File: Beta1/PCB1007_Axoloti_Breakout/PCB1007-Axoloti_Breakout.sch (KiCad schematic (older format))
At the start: 35 parts, among them J1 Axoloti_40Pin, U10 OLED_128x32_I2C, U1000 MCP3008T-I/SL, U2 MCP3008T-I/SL, U20 OLED_128x32_I2C, U30 OLED_128x32_I2C, U40 OLED_128x32_I2C, U5 I2C_1x4MUX_TCA9546A

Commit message: SCH+Route complete
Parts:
- removed C1, C1000, C2: 0.1u, Capacitors_SMD:C_0603, symbol C
- removed JOY0, JOY1, JOY2, JOY3: XYJOY, Liberry:XY_JOY_254TA103B50B, symbol XYJOY
- removed RC0, RC10, RC20, RC30, RC40, RD0, RD10, RD20, RD30, RD40, RR0: 10K, Resistors_SMD:R_0603, symbol R
- removed RV0, RV1, RV2, RV3, RV4, RV5, RV6, RV7, RV_VOL1: POT, Liberry:RV09AF-40-20K-B10K, symbol POT
- removed U10, U20, U30, U40: OLED_128x32_I2C, Liberry:OLED_128x32, symbol OLED_128x32_I2C
- removed U1000, U2: MCP3008T-I/SL, Liberry:SOIC-16, symbol MCP3008T-I/SL
- removed U5: I2C_1x4MUX_TCA9546A, Liberry:SOIC-16_1.27x5.4, symbol I2C_1x4MUX_TCA9546A
- added JK0: USB-K, Liberry:USB-K_12401610E4_2A, symbol USB-K
- added TEST0, TEST1, TEST2: CONN_01X01, Liberry:TH_0.1_1x2_Jumper, symbol CONN_01X01
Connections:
- net labels added: JOY0, JOY1, JOY_SW, RX, TEST0, TEST1, TEST2, TX
- net labels removed: I2C_SCL0, I2C_SCL1, I2C_SCL2, I2C_SCL3, I2C_SDA0, I2C_SDA1, I2C_SDA2, I2C_SDA3, JOY_0_0, JOY_0_1, JOY_0_SW, JOY_1_0, JOY_1_1, JOY_2_0, JOY_2_1, JOY_3_0, JOY_3_1, JOY_K0, JOY_K1, P0, P1, P2, P3, P4, P5, P6, P7
- wire segments 204 -> 60

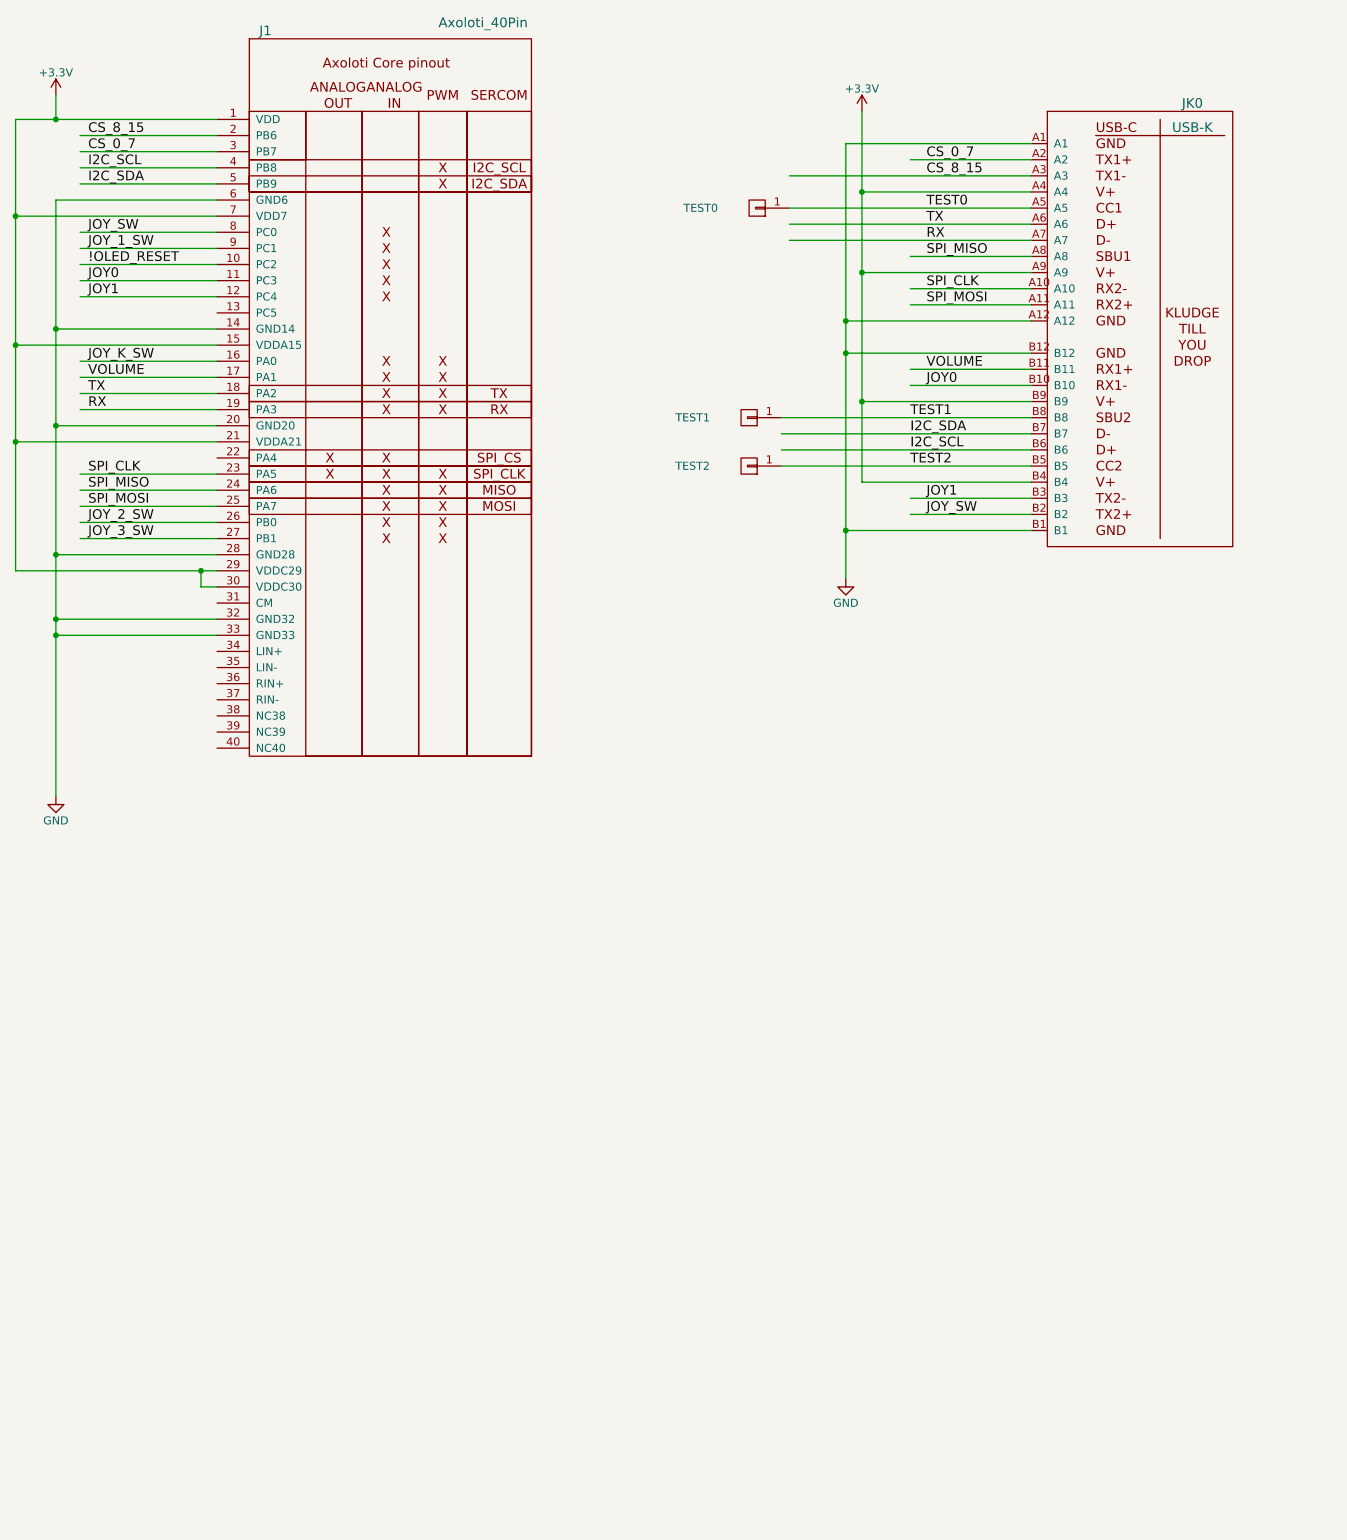
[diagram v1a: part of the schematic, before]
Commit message: Conversion to FFC WIP
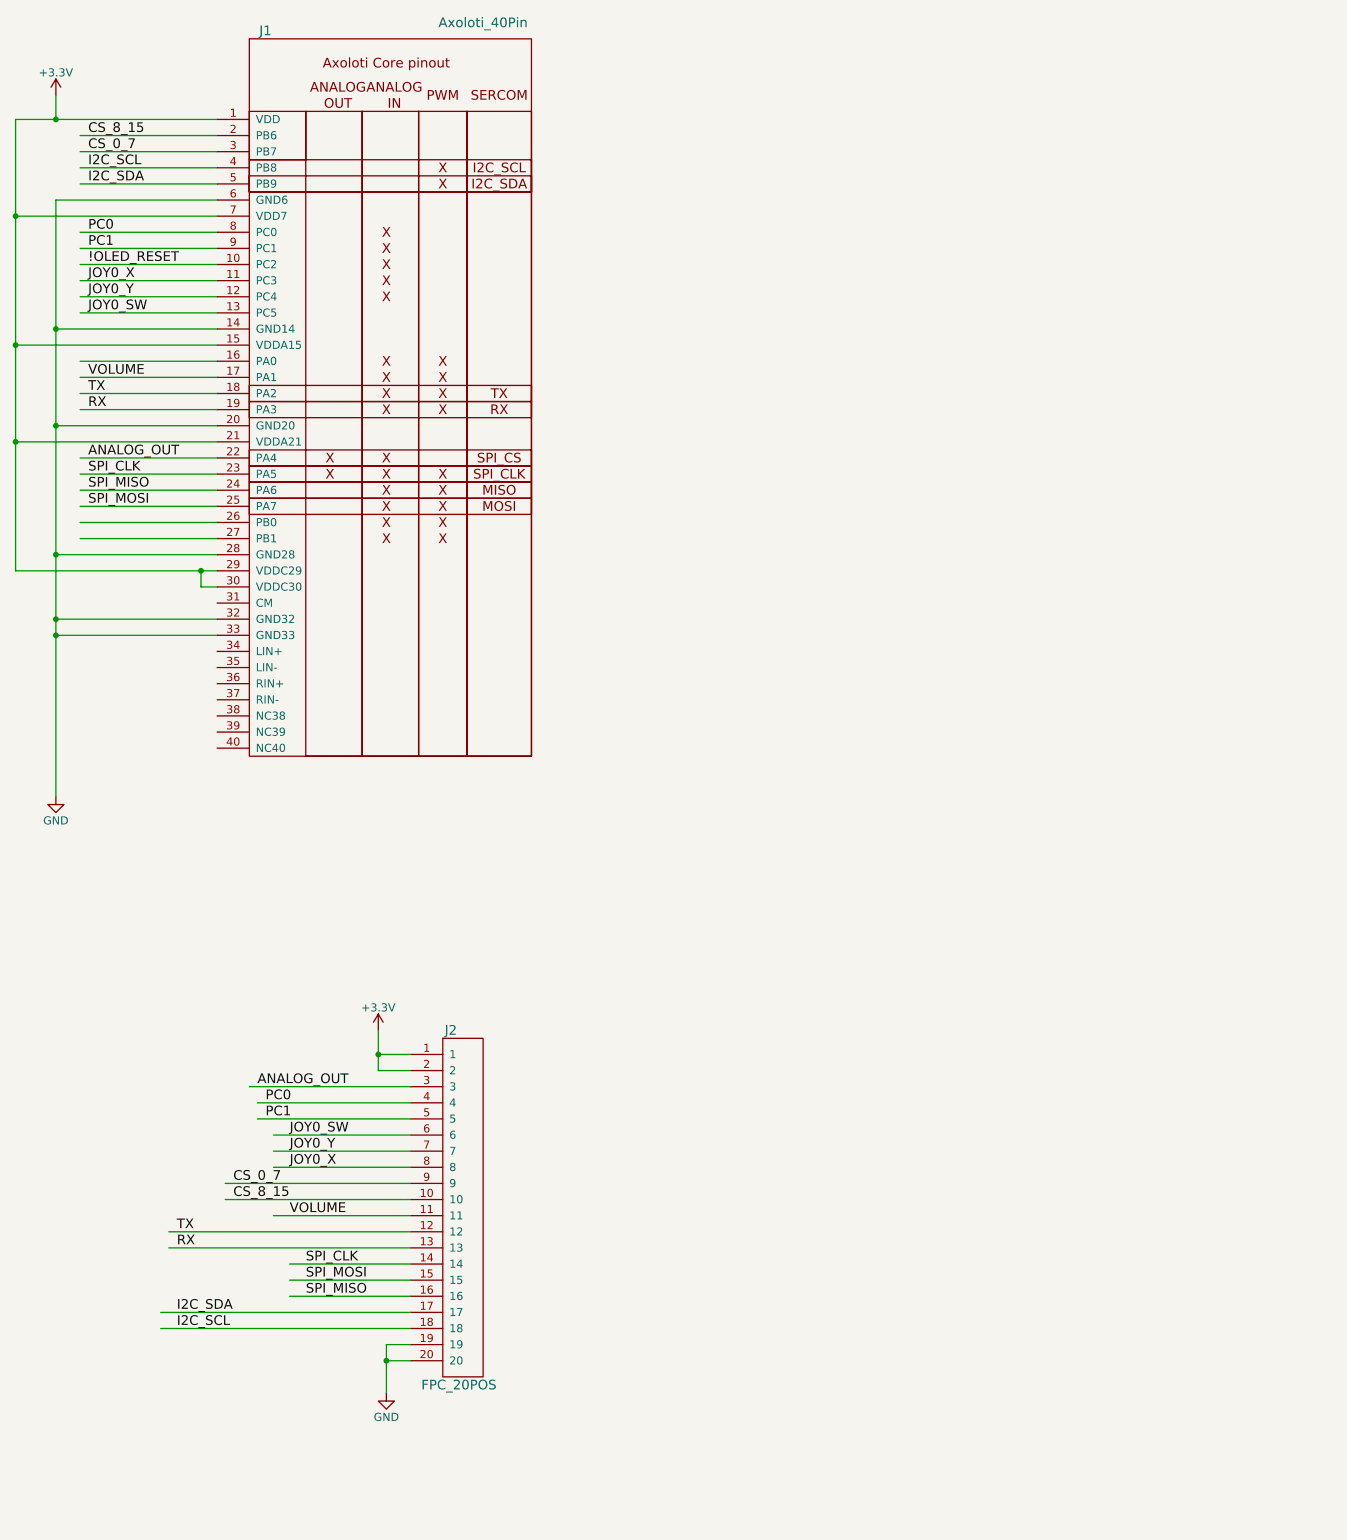
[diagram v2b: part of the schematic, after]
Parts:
- removed JK0: USB-K, Liberry:USB-K_12401610E4_2A, symbol USB-K
- removed TEST0, TEST1, TEST2: CONN_01X01, Liberry:TH_0.1_1x2_Jumper, symbol CONN_01X01
- added J2: FPC_20POS, Liberry:FFC_1MM_20POS_MOLEX_52271-2079, symbol FPC_20POS
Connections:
- net labels added: ANALOG_OUT, JOY0_SW, JOY0_X, JOY0_Y, PC0, PC1
- net labels removed: JOY0, JOY1, JOY_1_SW, JOY_2_SW, JOY_3_SW, JOY_K_SW, JOY_SW, TEST0, TEST1, TEST2
- wire segments 60 -> 58
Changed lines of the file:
@@
 Text Label 15100 4300 0    60   ~ 0
 SPI_CLK
-Text Label 15100 2800 0    60   ~ 0
-JOY_SW
-Text Label 15100 2900 0    60   ~ 0
-JOY_1_SW
-Text Label 15100 4600 0    60   ~ 0
-JOY_2_SW
 Text Label 15100 2300 0    60   ~ 0
 CS_0_7
@@
 Text Label 15100 3000 0    60   ~ 0
 !OLED_RESET
+Text Label 15100 3700 0    60   ~ 0
+VOLUME
+Text Label 15100 3100 0    60   ~ 0
+JOY0_X
+Text Label 15100 3200 0    60   ~ 0
+JOY0_Y
+Text Label 16450 9300 0    60   ~ 0
+SPI_MOSI
+Text Label 16450 9200 0    60   ~ 0
+SPI_CLK
+Text Label 16000 8700 0    60   ~ 0
+CS_0_7
+Text Label 16350 8900 0    60   ~ 0
+VOLUME
+Text Label 16350 8600 0    60   ~ 0
+JOY0_X
+Text Label 15650 9600 0    60   ~ 0
+I2C_SCL
+Text Label 15650 9500 0    60   ~ 0
+I2C_SDA
+Text Label 15650 9100 0    60   ~ 0
+RX
+Text Label 15650 9000 0    60   ~ 0
+TX
+Text Label 16000 8800 0    60   ~ 0
+CS_8_15
+Text Label 16450 9400 0    60   ~ 0
+SPI_MISO
+Text Label 15100 3800 0    60   ~ 0
+TX
+Text Label 15100 3900 0    60   ~ 0
+RX
+$Comp
+L +3.3V #PWR?
+U 1 1 596EA01A
+P 16900 7750
+F 0 "#PWR?" H 16900 7600 50  0001 C CNN
+F 1 "+3.3V" H 16900 7890 50  0000 C CNN
+F 2 "" H 16900 7750 50  0000 C CNN
+F 3 "" H 16900 7750 50  0000 C CNN
+	1    16900 7750
+	1    0    0    -1
+$EndComp
+$Comp
+L GND #PWR?
+U 1 1 596EA0DD
+P 16950 10000
+F 0 "#PWR?" H 16950 9750 50  0001 C CNN
+F 1 "GND" H 16950 9850 50  0000 C CNN
+F 2 "" H 16950 10000 50  0000 C CNN
+F 3 "" H 16950 10000 50  0000 C CNN
+	1    16950 10000
+	1    0    0    -1
+$EndComp
+$Comp
+L FPC_20POS J2
+U 1 1 596EA301
+P 17300 7900
+F 0 "J2" H 17350 8050 60  0000 C CNN
+F 1 "FPC_20POS" H 17400 5850 60  0000 C CNN
+F 2 "Liberry:FFC_1MM_20POS_MOLEX_52271-2079" H 17100 7450 60  0001 C CNN
+F 3 "" H 17100 7450 60  0001 C CNN
+	1    17300 7900
+	1    0    0    -1
+$EndComp
+Text Label 16350 8500 0    60   ~ 0
+JOY0_Y
+Text Label 15100 3300 0    60   ~ 0
+JOY0_SW
+Text Label 16350 8400 0    60   ~ 0
+JOY0_SW
+Text Label 15100 2800 0    60   ~ 0
+PC0
+Text Label 15100 4200 0    60   ~ 0
+ANALOG_OUT
+Text Label 16150 8100 0    60   ~ 0
+ANALOG_OUT
+Text Label 15100 2900 0    60   ~ 0
+PC1
+Text Label 16200 8200 0    60   ~ 0
+PC0
+Text Label 16200 8300 0    60   ~ 0
+PC1
 Wire Wire Line
 	15050 2500 15900 2500
@@
 Wire Wire Line
 	15050 2900 15900 2900
-Wire Wire Line
-	15050 4600 15900 4600
 Wire Wire Line
 	15050 2300 15900 2300
@@
 Wire Wire Line
 	15900 4700 15050 4700
-Text Label 15100 4700 0    60   ~ 0
-JOY_3_SW
-Text Label 15100 3700 0    60   ~ 0
-VOLUME
 Wire Wire Line
 	15050 3700 15900 3700
-Text Label 15100 3100 0    60   ~ 0
-JOY0
-Text Label 15100 3200 0    60   ~ 0
-JOY1
-Text Label 15100 3600 0    60   ~ 0
-JOY_K_SW
 Wire Wire Line
 	15900 3100 15050 3100
@@
 	15900 3200 15050 3200
 Wire Wire Line
+	17100 9300 16350 9300
+Wire Wire Line
+	17100 9200 16350 9200
+Wire Wire Line
+	16350 9400 17100 9400
+Wire Wire Line
+	15600 9100 17100 9100
+Wire Wire Line
+	15600 9000 17100 9000
+Wire Wire Line
+	15950 8700 17100 8700
+Wire Wire Line
+	16250 8900 17100 8900
+Wire Wire Line
+	16250 8600 17100 8600
+Wire Wire Line
+	15550 9500 17100 9500
+Wire Wire Line
+	15550 9600 17100 9600
+Wire Wire Line
+	15900 3800 15050 3800
+Wire Wire Line
+	15900 3900 15050 3900
+Wire Wire Line
+	17100 7900 16900 7900
+Wire Wire Line
+	16900 7750 16900 8000
+Wire Wire Line
+	16900 8000 17100 8000
+Connection ~ 16900 7900
+Wire Wire Line
+	17100 9700 16950 9700
+Wire Wire Line
+	16950 9700 16950 10000
+Wire Wire Line
+	16950 9800 17100 9800
+Connection ~ 16950 9800
+Wire Wire Line
+	15950 8800 17100 8800
+Wire Wire Line
+	16250 8500 17100 8500
+Wire Wire Line
+	15050 3300 15900 3300
+Wire Wire Line
+	16250 8400 17100 8400
+Wire Wire Line
+	15050 4600 15900 4600
+Wire Wire Line
 	15900 3600 15050 3600
-$Comp
-L USB-K JK0
-U 1 1 59612141
-P 20950 3450
-F 0 "JK0" H 21950 4900 60  0000 C CNN
-F 1 "USB-K" H 21950 4750 60  0000 C CNN
-F 2 "Liberry:USB-K_12401610E4_2A" H 21000 3350 60  0001 C CNN
-F 3 "" H 21000 3350 60  0001 C CNN
-	1    20950 3450
-	1    0    0    -1
-$EndComp
-$Comp
-L GND #PWR03
-U 1 1 59612148
-P 19800 4950
-F 0 "#PWR03" H 19800 4700 50  0001 C CNN
-F 1 "GND" H 19800 4800 50  0000 C CNN
-F 2 "" H 19800 4950 50  0000 C CNN
-F 3 "" H 19800 4950 50  0000 C CNN
-	1    19800 4950
-	1    0    0    -1
-$EndComp
-$Comp
-L +3.3V #PWR04
-U 1 1 5961214E
-P 19900 2050
-F 0 "#PWR04" H 19900 1900 50  0001 C CNN
-F 1 "+3.3V" H 19900 2190 50  0000 C CNN
-F 2 "" H 19900 2050 50  0000 C CNN
-F 3 "" H 19900 2050 50  0000 C CNN
-	1    19900 2050
-	1    0    0    -1
-$EndComp
-Wire Wire Line
-	19800 4650 20950 4650
-Wire Wire Line
-	19800 2250 19800 4950
-Wire Wire Line
-	20950 3550 19800 3550
-Connection ~ 19800 4650
-Wire Wire Line
-	20950 3350 19800 3350
-Connection ~ 19800 3550
-Wire Wire Line
-	20950 2250 19800 2250
-Connection ~ 19800 3350
-Wire Wire Line
-	20950 2550 19900 2550
-Wire Wire Line
-	19900 2050 19900 4350
-Wire Wire Line
-	19900 3050 20950 3050
-Connection ~ 19900 2550
-Wire Wire Line
-	19900 3850 20950 3850
-Connection ~ 19900 3050
-Wire Wire Line
-	19900 4350 20950 4350
-Connection ~ 19900 3850
-Wire Wire Line
-	20950 3250 20200 3250
-Wire Wire Line
-	20950 3150 20200 3150
-Wire Wire Line
-	20200 2950 20950 2950
-Wire Wire Line
-	19450 2850 20950 2850
-Wire Wire Line
-	19450 2750 20950 2750
-Wire Wire Line
-	19450 2650 20950 2650
-Wire Wire Line
-	19450 2450 20950 2450
-Wire Wire Line
-	20950 2350 20200 2350
-Wire Wire Line
-	20950 3650 20200 3650
-Wire Wire Line
-	20950 3750 20200 3750
-Wire Wire Line
-	19400 3950 20950 3950
-Wire Wire Line
-	19400 4050 20950 4050
-Wire Wire Line
-	19400 4150 20950 4150
-Wire Wire Line
-	19400 4250 20950 4250
-Wire Wire Line
-	20950 4450 20200 4450
-Wire Wire Line
-	20950 4550 20200 4550
-Text Label 20300 3250 0    60   ~ 0
-SPI_MOSI
-Text Label 20300 3150 0    60   ~ 0
-SPI_CLK
-Text Label 20300 2350 0    60   ~ 0
-CS_0_7
-$Comp
-L CONN_01X01 TEST0
-U 1 1 59612194
-P 19250 2650
-F 0 "TEST0" H 19600 2650 50  0000 C CNN
-F 1 "CONN_01X01" V 19350 2650 50  0001 C CNN
-F 2 "Liberry:TH_0.1_1x2_Jumper" H 19250 2650 50  0001 C CNN
-F 3 "" H 19250 2650 50  0000 C CNN
-F 4 "PCB" H 19250 2650 60  0001 C CNN "MFG"
-F 5 "ON_PCB" H 19250 2650 60  0001 C CNN "MPN"
-	1    19250 2650
-	-1   0    0    1
-$EndComp
-Text Label 20300 3650 0    60   ~ 0
-VOLUME
-Text Label 20300 3750 0    60   ~ 0
-JOY0
-Text Label 20300 4550 0    60   ~ 0
-JOY_SW
-Text Label 20300 4450 0    60   ~ 0
-JOY1
-$Comp
-L CONN_01X01 TEST1
-U 1 1 596121B3
-P 19200 3950
-F 0 "TEST1" H 19550 3950 50  0000 C CNN
-F 1 "CONN_01X01" V 19300 3950 50  0001 C CNN
-F 2 "Liberry:TH_0.1_1x2_Jumper" H 19200 3950 50  0001 C CNN
-F 3 "" H 19200 3950 50  0000 C CNN
-F 4 "PCB" H 19200 3950 60  0001 C CNN "MFG"
-F 5 "ON_PCB" H 19200 3950 60  0001 C CNN "MPN"
-	1    19200 3950
-	-1   0    0    1
-$EndComp
-$Comp
-L CONN_01X01 TEST2
-U 1 1 596121BC
-P 19200 4250
-F 0 "TEST2" H 19550 4250 50  0000 C CNN
-F 1 "CONN_01X01" V 19300 4250 50  0001 C CNN
-F 2 "Liberry:TH_0.1_1x2_Jumper" H 19200 4250 50  0001 C CNN
-F 3 "" H 19200 4250 50  0000 C CNN
-F 4 "PCB" H 19200 4250 60  0001 C CNN "MFG"
-F 5 "ON_PCB" H 19200 4250 60  0001 C CNN "MPN"
-	1    19200 4250
-	-1   0    0    1
-$EndComp
-Text Label 20200 4150 0    60   ~ 0
-I2C_SCL
-Text Label 20200 4250 0    60   ~ 0
-TEST2
-Text Label 20200 4050 0    60   ~ 0
-I2C_SDA
-Text Label 20200 3950 0    60   ~ 0
-TEST1
-Text Label 20300 2850 0    60   ~ 0
-RX
-Text Label 20300 2750 0    60   ~ 0
-TX
-Text Label 20300 2650 0    60   ~ 0
-TEST0
-Text Label 20300 2450 0    60   ~ 0
-CS_8_15
-Text Label 20300 2950 0    60   ~ 0
-SPI_MISO
-Wire Wire Line
-	15900 3800 15050 3800
-Wire Wire Line
-	15900 3900 15050 3900
-Text Label 15100 3800 0    60   ~ 0
-TX
-Text Label 15100 3900 0    60   ~ 0
-RX
+Wire Wire Line
+	15900 4200 15050 4200
+Wire Wire Line
+	16100 8100 17100 8100
+Wire Wire Line
+	16150 8200 17100 8200
+Wire Wire Line
+	16150 8300 17100 8300
 $EndSCHEMATC

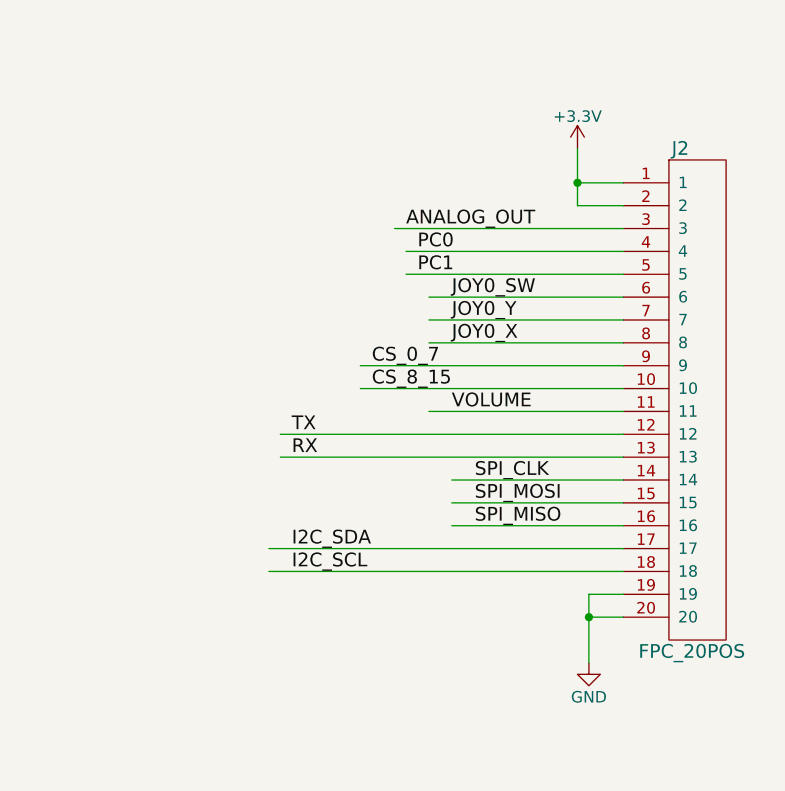
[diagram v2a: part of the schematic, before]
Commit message: Added 20 pos FFC
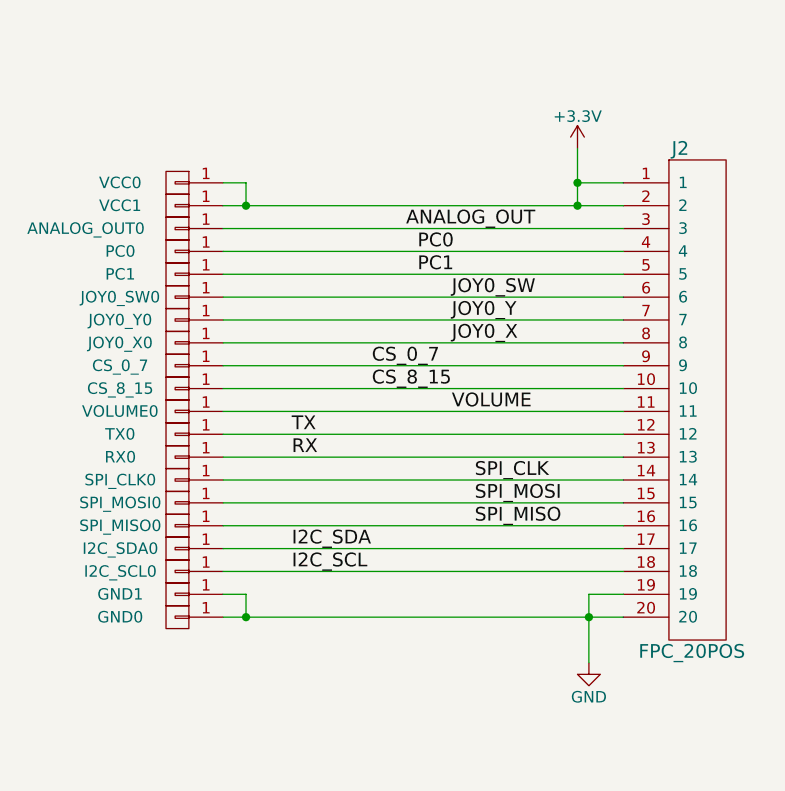
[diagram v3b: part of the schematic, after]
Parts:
- added ANALOG_OUT0, CS_0_7, CS_8_15, GND0, GND1, I2C_SCL0, I2C_SDA0, JOY0_SW0, JOY0_X0, JOY0_Y0, PC0, PC1, RX0, SPI_CLK0, SPI_MISO0, SPI_MOSI0, TX0, VCC0, VCC1, VOLUME0: CONN_01X01, Liberry:single_0.1, symbol CONN_01X01
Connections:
- wire segments 58 -> 62
